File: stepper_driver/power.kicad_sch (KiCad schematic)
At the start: 8 parts, among them Q1 MOSFET-N-CH, Q2 MOSFET-P-CH-EN-BUK6D120-60PX

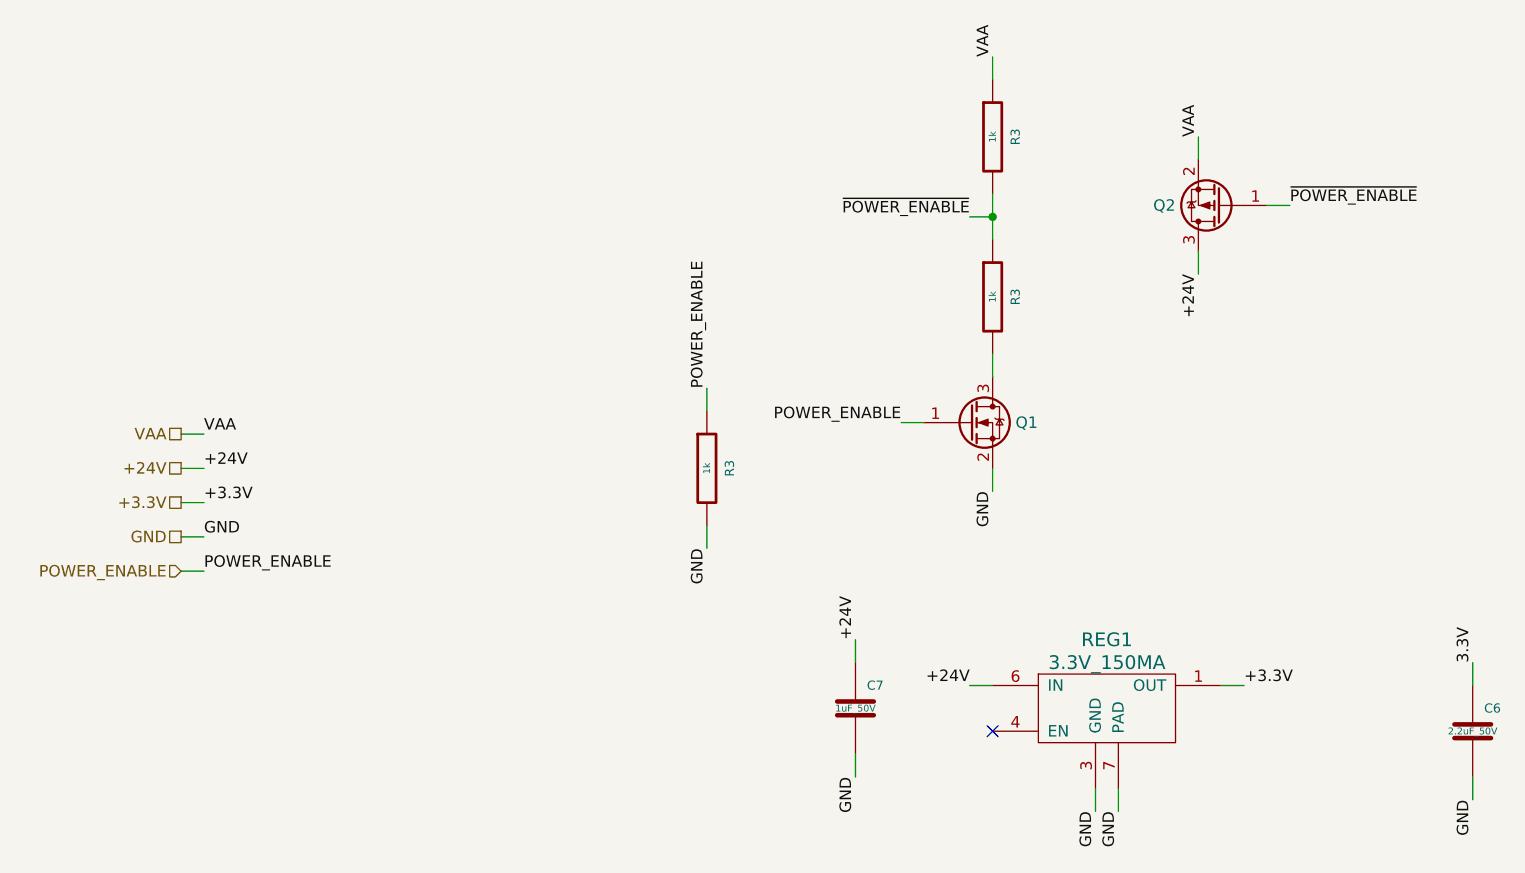
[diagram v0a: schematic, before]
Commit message: power_enable -> standby
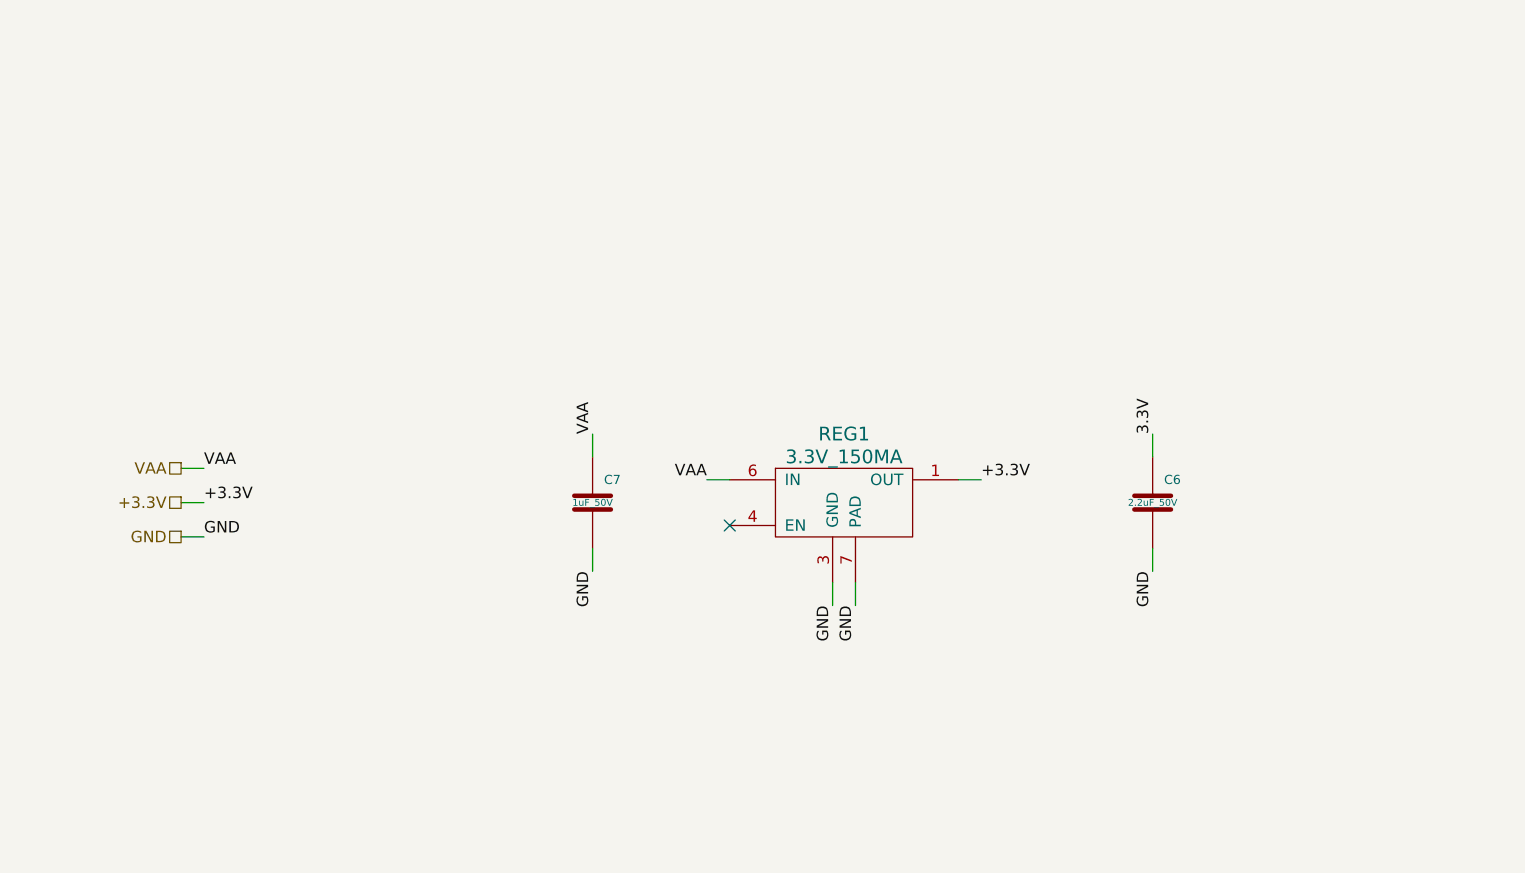
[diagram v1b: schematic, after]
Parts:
- removed Q1: MOSFET-N-CH, Janelia:XFDFN-3, symbol Janelia:MOSFET-N-CH-EN-CSD17483F4
- removed Q2: MOSFET-P-CH-EN-BUK6D120-60PX, Janelia:DFN2020-MD6-MOSFET, symbol Janelia:MOSFET-P-CH-EN-BUK6D120-60PX
- removed R3 (x3): 1k, Janelia:R_0402_1005Metric, symbol Janelia:R_1k_0402
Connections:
- net +24V is gone; now on net VAA: C7.1, REG1.6 (IN)
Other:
- moved on the sheet: C6, C7, REG1

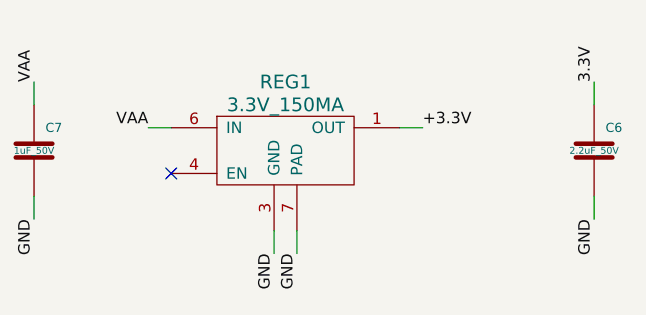
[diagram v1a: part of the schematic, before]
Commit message: Fix ERC errors
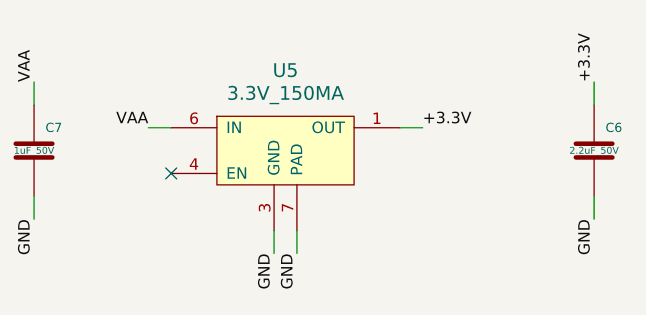
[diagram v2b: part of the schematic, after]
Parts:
- removed REG1: 3.3V_150MA, Janelia:SON65P200X200X80-7N, symbol Janelia:CONV_DC_DC_3.3V_150MA
- added U5: 3.3V_150MA, Janelia:SON65P200X200X80-7N, symbol Janelia:Regulator_Linear_3.3V_150MA_30Vin
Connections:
- net 3.3V is gone; now on net +3.3V: C6.1
- net +3.3V: now also U5.1 (OUT)
- net GND: now also U5.3 (GND), U5.7 (PAD)
- net VAA: now also U5.6 (IN)
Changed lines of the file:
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@@
     (effects (font (size 1.27 1.27)) (justify left bottom))
   )
-  (label "3.3V" (at 167.64 88.9 90) (fields_autoplaced)
+  (label "+3.3V" (at 167.64 88.9 90) (fields_autoplaced)
     (effects (font (size 1.27 1.27)) (justify left bottom))
   )
@@
     )
   )
-  (symbol (lib_id "Janelia:CONV_DC_DC_3.3V_150MA") (at 133.35 93.98 0) (unit 1)
-    (in_bom yes) (on_board yes) (dnp no) (fields_autoplaced)
-    (property "Reference" "REG1" (at 133.35 88.9 0)
-      (effects (font (size 1.524 1.524)))
-    )
-    (property "Value" "3.3V_150MA" (at 133.35 91.44 0)
-      (effects (font (size 1.524 1.524)))
-    )
-    (property "Footprint" "Janelia:SON65P200X200X80-7N" (at 133.35 83.82 0)
-      (effects (font (size 1.524 1.524)) hide)
-    )
-    (property "Datasheet" "" (at 133.35 93.98 0)
-      (effects (font (size 1.524 1.524)) hide)
-    )
-    (property "Vendor" "Digi-Key" (at 133.35 78.74 0)
-      (effects (font (size 1.27 1.27)) hide)
-    )
-    (property "Vendor Part Number" "296-40930-1-ND" (at 133.35 81.28 0)
-      (effects (font (size 1.27 1.27)) hide)
-    )
-    (property "Manufacturer" "Texas Instruments" (at 133.35 71.12 0)
-      (effects (font (size 1.27 1.27)) hide)
-    )
-    (property "Manufacturer Part Number" "TPS70933DRVR" (at 133.35 73.66 0)
-      (effects (font (size 1.27 1.27)) hide)
-    )
-    (property "Package" " 6WSON" (at 133.35 68.58 0)
-      (effects (font (size 1.27 1.27)) hide)
-    )
-    (property "Description" "IC REG LINEAR 3.3V 150MA" (at 133.35 76.2 0)
-      (effects (font (size 1.27 1.27)) hide)
-    )
-    (pin "1")
-    (pin "3")
-    (pin "4")
-    (pin "6")
-    (pin "7")
-    (instances
-      (project "stepper_driver"
-        (path "/cc457ebc-4af6-4663-b19f-8cb38f061cb4"
-          (reference "REG1") (unit 1)
-        )
-        (path "/cc457ebc-4af6-4663-b19f-8cb38f061cb4/4100450f-855b-4653-a714-110b9fa85f89"
-          (reference "REG1") (unit 1)
-        )
-      )
-    )
-  )
   (symbol (lib_id "Janelia:C_1uF_50V_0603") (at 105.41 96.52 0) (unit 1)
     (in_bom yes) (on_board yes) (dnp no)
@@
         )
       )
+    )
+  )
+  (symbol (lib_id "Janelia:Regulator_Linear_3.3V_150MA_30Vin") (at 133.35 93.98 0) (unit 1)
+    (in_bom yes) (on_board yes) (dnp no) (fields_autoplaced)
+    (property "Reference" "U5" (at 133.35 87.63 0)
+      (effects (font (size 1.524 1.524)))
+    )
+    (property "Value" "3.3V_150MA" (at 133.35 90.17 0)
+      (effects (font (size 1.524 1.524)))
+    )
+    (property "Footprint" "Janelia:SON65P200X200X80-7N" (at 133.35 83.82 0)
+      (effects (font (size 1.524 1.524)) hide)
+    )
+    (property "Datasheet" "" (at 133.35 93.98 0)
+      (effects (font (size 1.524 1.524)) hide)
+    )
+    (property "Vendor" "Digi-Key" (at 133.35 78.74 0)
+      (effects (font (size 1.27 1.27)) hide)
+    )
+    (property "Vendor Part Number" "296-40930-1-ND" (at 133.35 81.28 0)
+      (effects (font (size 1.27 1.27)) hide)
+    )
+    (property "Manufacturer" "Texas Instruments" (at 133.35 71.12 0)
+      (effects (font (size 1.27 1.27)) hide)
+    )
+    (property "Manufacturer Part Number" "TPS70933DRVR" (at 133.35 73.66 0)
+      (effects (font (size 1.27 1.27)) hide)
+    )
+    (property "Package" " 6WSON" (at 133.35 68.58 0)
+      (effects (font (size 1.27 1.27)) hide)
+    )
+    (property "Description" "IC REG LINEAR 3.3V 150MA" (at 133.35 76.2 0)
+      (effects (font (size 1.27 1.27)) hide)
+    )
+    (property "Sim.Enable" "0" (at 133.35 93.98 0)
+      (effects (font (size 1.27 1.27)) hide)
+    )
+    (pin "1")
+    (pin "3")
+    (pin "4")
+    (pin "6")
+    (pin "7")
+    (instances
+      (project "stepper_driver"
+        (path "/cc457ebc-4af6-4663-b19f-8cb38f061cb4/4100450f-855b-4653-a714-110b9fa85f89"
+          (reference "U5") (unit 1)
+        )
+      )
